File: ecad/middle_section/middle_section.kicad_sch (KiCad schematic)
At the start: 12 parts, among them U1 ADS7830, U2 LM4040DBZ-3

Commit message: [WIP]
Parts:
- removed C1, C3: C_Polarized, Capacitor_SMD:CP_Elec_4x5.7, symbol Device:C_Polarized
- added C1, C3: 2u2, Capacitor_SMD:C_0805_2012Metric, symbol Device:C
- added J1: JST SH, Connector_JST:JST_SH_BM04B-SRSS-TB_1x04-1MP_P1.00mm_Vertical, symbol Connector_Generic:Conn_01x04
- added JP1, JP2: ~, Jumper:SolderJumper-3_P1.3mm_Open_RoundedPad1.0x1.5mm, symbol Jumper:SolderJumper_3_Bridged123
- C2, C4: value C -> 100n
- R1: value R -> 100
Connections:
- net +3V0: now also C1.1
- net +3V3: now also C3.1, J1.1 (Pin_1), JP1.1 (A), JP2.1 (A)
- net GND: now also C1.2, C3.2, J1.4 (Pin_4), JP1.3 (B), JP2.3 (B)
- net A1: now reaches U1.12 (A0)
- net A1: now also JP2.2 (C)
- net A0: now reaches U1.13 (A1)
- net A0: now also JP1.2 (C)
- net SCK: now reaches U1.14 (SCL)
- net SCK: now also J1.3 (Pin_3)
- net SDA: now reaches U1.15 (SDA)
- net SDA: now also J1.2 (Pin_2)

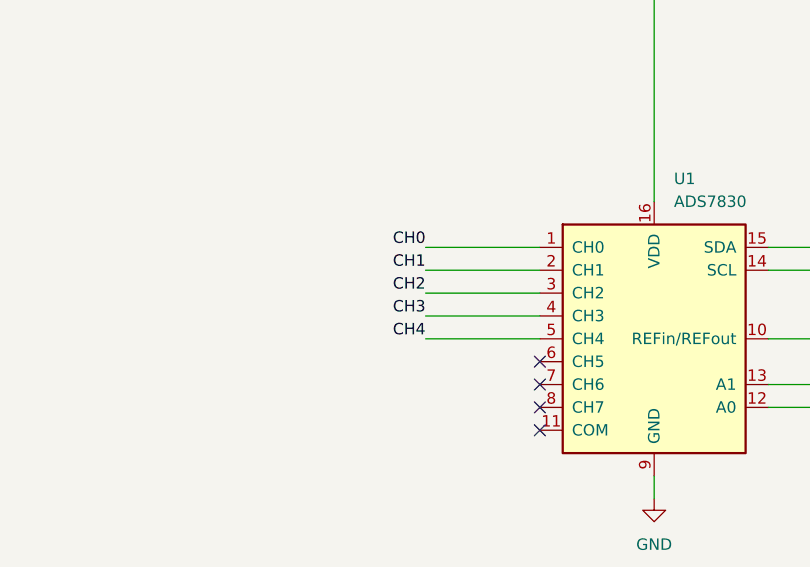
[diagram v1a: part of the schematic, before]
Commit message: Finishes up Middle Section
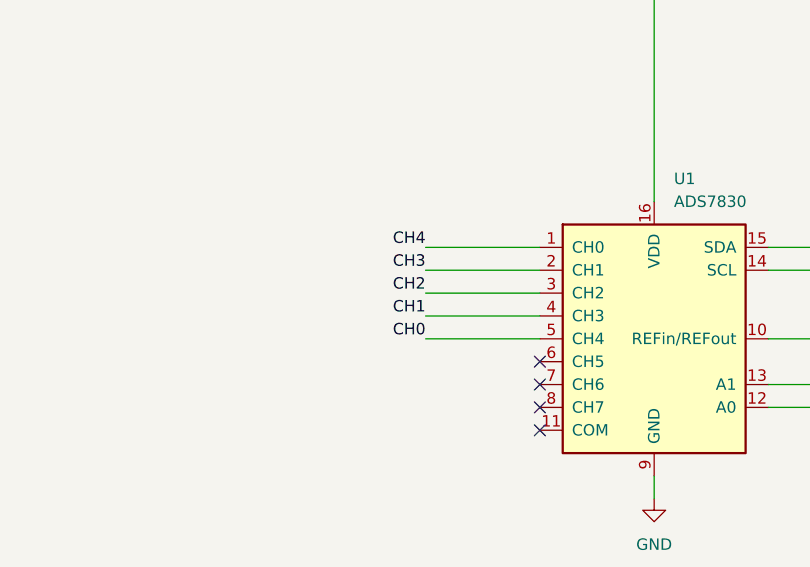
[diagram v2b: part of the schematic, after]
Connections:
- net CH0: now also U1.5 (CH4); no longer U1.1 (CH0)
- net CH1: now also U1.4 (CH3); no longer U1.2 (CH1)
- net CH3: now also U1.2 (CH1); no longer U1.4 (CH3)
- net CH4: now also U1.1 (CH0); no longer U1.5 (CH4)
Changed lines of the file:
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@@
 	)
 	(label "CH3"
-		(at 190.5 58.42 180)
+		(at 190.5 53.34 180)
 		(fields_autoplaced yes)
 		(effects
@@
 	)
 	(label "CH4"
-		(at 190.5 60.96 180)
+		(at 190.5 50.8 180)
 		(fields_autoplaced yes)
 		(effects
@@
 	)
 	(label "CH1"
-		(at 190.5 53.34 180)
+		(at 190.5 58.42 180)
 		(fields_autoplaced yes)
 		(effects
@@
 	)
 	(label "CH0"
-		(at 190.5 50.8 180)
+		(at 190.5 60.96 180)
 		(fields_autoplaced yes)
 		(effects

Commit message: Updates boards
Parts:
- added R2: 100, Resistor_SMD:R_0603_1608Metric, symbol Device:R
- J1: footprint Connector_JST:JST_SH_BM04B-SRSS-TB_1x04-1MP_P1.00mm_Vertical -> woodpecker:JST_SH_BM04B-SRSS-TB_1x04-1MP_P1.00mm_Vertical
- JP1, JP2: footprint Jumper:SolderJumper-3_P1.3mm_Open_RoundedPad1.0x1.5mm -> Jumper:SolderJumper-3_P2.0mm_Open_TrianglePad1.0x1.5mm
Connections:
- net +3V3: now also R2.1; no longer JP1.1 (A), JP2.1 (A)
- new net: JP1.1 (A), JP2.1 (A), R2.2
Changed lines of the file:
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@@
 	)
 	(junction
+		(at 267.97 66.04)
+		(diameter 0)
+		(color 0 0 0 0)
+	)
+	(junction
 		(at 107.95 36.83)
 		(diameter 0)
@@
 	(wire
 		(pts
+			(xy 247.65 66.04) (xy 247.65 76.2)
+		)
+		(stroke
+			(width 0)
+			(type default)
+		)
+	)
+	(wire
+		(pts
 			(xy 151.13 102.87) (xy 154.94 102.87)
 		)
@@
 	(wire
 		(pts
+			(xy 267.97 66.04) (xy 267.97 76.2)
+		)
+		(stroke
+			(width 0)
+			(type default)
+		)
+	)
+	(wire
+		(pts
 			(xy 120.65 110.49) (xy 120.65 106.68)
 		)
@@
 	(wire
 		(pts
-			(xy 228.6 68.58) (xy 234.95 68.58)
+			(xy 247.65 66.04) (xy 267.97 66.04)
 		)
 		(stroke
@@
 	(wire
 		(pts
-			(xy 267.97 72.39) (xy 267.97 76.2)
+			(xy 228.6 68.58) (xy 234.95 68.58)
 		)
 		(stroke
@@
 	(wire
 		(pts
+			(xy 267.97 52.07) (xy 267.97 54.61)
+		)
+		(stroke
+			(width 0)
+			(type default)
+		)
+	)
+	(wire
+		(pts
 			(xy 95.25 95.25) (xy 95.25 99.06)
 		)
@@
 	(wire
 		(pts
-			(xy 247.65 72.39) (xy 247.65 76.2)
-		)
-		(stroke
-			(width 0)
-			(type default)
-		)
-	)
-	(wire
-		(pts
 			(xy 175.26 102.87) (xy 179.07 102.87)
 		)
@@
 	(wire
 		(pts
+			(xy 267.97 66.04) (xy 267.97 62.23)
+		)
+		(stroke
+			(width 0)
+			(type default)
+		)
+	)
+	(wire
+		(pts
 			(xy 215.9 22.86) (xy 242.57 22.86)
 		)
@@
 	(symbol
 		(lib_id "power:+3V3")
-		(at 267.97 72.39 0)
+		(at 267.97 52.07 0)
 		(unit 1)
 		(exclude_from_sim no)
@@
 		(fields_autoplaced yes)
 		(property "Reference" "#PWR022"
-			(at 267.97 76.2 0)
+			(at 267.97 55.88 0)
 			(effects
 				(font
@@
 		)
 		(property "Value" "+3V3"
-			(at 267.97 67.31 0)
+			(at 267.97 46.99 0)
 			(effects
 				(font
@@
 		)
 		(property "Footprint" ""
-			(at 267.97 72.39 0)
+			(at 267.97 52.07 0)
 			(effects
 				(font
@@
 		)
 		(property "Datasheet" ""
-			(at 267.97 72.39 0)
+			(at 267.97 52.07 0)
 			(effects
 				(font
@@
 		)
 		(property "Description" "Power symbol creates a global label with name \"+3V3\""
-			(at 267.97 72.39 0)
+			(at 267.97 52.07 0)
 			(effects
 				(font
@@
 	)
 	(symbol
-		(lib_id "power:+3V3")
-		(at 247.65 72.39 0)
+		(lib_id "Jumper:SolderJumper_3_Bridged123")
+		(at 267.97 81.28 270)
 		(unit 1)
 		(exclude_from_sim no)
@@
 		(dnp no)
 		(fields_autoplaced yes)
-		(property "Reference" "#PWR021"
-			(at 247.65 76.2 0)
+		(property "Reference" "JP2"
+			(at 270.51 80.0099 90)
 			(effects
 				(font
 					(size 1.27 1.27)
 				)
-				(hide yes)
+				(justify left)
 			)
 		)
-		(property "Value" "+3V3"
-			(at 247.65 67.31 0)
+		(property "Value" "~"
+			(at 270.51 82.5499 90)
 			(effects
 				(font
 					(size 1.27 1.27)
 				)
+				(justify left)
+				(hide yes)
 			)
 		)
-		(property "Footprint" ""
-			(at 247.65 72.39 0)
+		(property "Footprint" "Jumper:SolderJumper-3_P2.0mm_Open_TrianglePad1.0x1.5mm"
+			(at 267.97 81.28 0)
 			(effects
 				(font
@@
 			)
 		)
-		(property "Datasheet" ""
-			(at 247.65 72.39 0)
+		(property "Datasheet" "~"
+			(at 267.97 81.28 0)
 			(effects
 				(font
@@
 			)
 		)
-		(property "Description" "Power symbol creates a global label with name \"+3V3\""
-			(at 247.65 72.39 0)
+		(property "Description" "Solder Jumper, 3-pole, pins 1+2+3 closed/bridged"
+			(at 267.97 81.28 0)
 			(effects
 				(font
@@
 			)
 		)
+		(pin "3"
+		)
 		(pin "1"
 		)
+		(pin "2"
+		)
 		(instances
 			(project "middle_section"
 				(path "/15a112d2-e643-4be2-b8ef-4d676777cd27"
-					(reference "#PWR021")
+					(reference "JP2")
 					(unit 1)
 				)
@@
 	)
 	(symbol
-		(lib_id "Jumper:SolderJumper_3_Bridged123")
-		(at 267.97 81.28 270)
+		(lib_id "power:+3V0")
+		(at 147.32 95.25 0)
 		(unit 1)
 		(exclude_from_sim no)
@@
 		(dnp no)
 		(fields_autoplaced yes)
-		(property "Reference" "JP2"
-			(at 270.51 80.0099 90)
+		(property "Reference" "#PWR017"
+			(at 147.32 99.06 0)
 			(effects
 				(font
 					(size 1.27 1.27)
 				)
-				(justify left)
+				(hide yes)
 			)
 		)
-		(property "Value" "~"
-			(at 270.51 82.5499 90)
+		(property "Value" "+3V0"
+			(at 147.32 90.17 0)
 			(effects
 				(font
 					(size 1.27 1.27)
 				)
-				(justify left)
-				(hide yes)
 			)
 		)
-		(property "Footprint" "Jumper:SolderJumper-3_P1.3mm_Open_RoundedPad1.0x1.5mm"
-			(at 267.97 81.28 0)
+		(property "Footprint" ""
+			(at 147.32 95.25 0)
 			(effects
 				(font
@@
 			)
 		)
-		(property "Datasheet" "~"
-			(at 267.97 81.28 0)
+		(property "Datasheet" ""
+			(at 147.32 95.25 0)
 			(effects
 				(font
@@
 			)
 		)
-		(property "Description" "Solder Jumper, 3-pole, pins 1+2+3 closed/bridged"
-			(at 267.97 81.28 0)
+		(property "Description" "Power symbol creates a global label with name \"+3V0\""
+			(at 147.32 95.25 0)
 			(effects
 				(font
@@
 			)
 		)
-		(pin "3"
-		)
 		(pin "1"
 		)
-		(pin "2"
-		)
 		(instances
 			(project "middle_section"
 				(path "/15a112d2-e643-4be2-b8ef-4d676777cd27"
-					(reference "JP2")
+					(reference "#PWR017")
 					(unit 1)
 				)
@@
 	(symbol
 		(lib_id "power:+3V0")
-		(at 147.32 95.25 0)
+		(at 137.16 22.86 0)
 		(unit 1)
 		(exclude_from_sim no)
@@
 		(dnp no)
 		(fields_autoplaced yes)
-		(property "Reference" "#PWR017"
-			(at 147.32 99.06 0)
+		(property "Reference" "#PWR09"
+			(at 137.16 26.67 0)
 			(effects
 				(font
@@
 		)
 		(property "Value" "+3V0"
-			(at 147.32 90.17 0)
+			(at 137.16 17.78 0)
 			(effects
 				(font
@@
 		)
 		(property "Footprint" ""
-			(at 147.32 95.25 0)
+			(at 137.16 22.86 0)
 			(effects
 				(font
@@
 		)
 		(property "Datasheet" ""
-			(at 147.32 95.25 0)
+			(at 137.16 22.86 0)
 			(effects
 				(font
@@
 		)
 		(property "Description" "Power symbol creates a global label with name \"+3V0\""
-			(at 147.32 95.25 0)
+			(at 137.16 22.86 0)
 			(effects
 				(font
@@
 			(project "middle_section"
 				(path "/15a112d2-e643-4be2-b8ef-4d676777cd27"
-					(reference "#PWR017")
+					(reference "#PWR09")
 					(unit 1)
 				)
@@
 	(symbol
 		(lib_id "power:+3V0")
-		(at 137.16 22.86 0)
+		(at 120.65 95.25 0)
 		(unit 1)
 		(exclude_from_sim no)
@@
 		(dnp no)
 		(fields_autoplaced yes)
-		(property "Reference" "#PWR09"
-			(at 137.16 26.67 0)
+		(property "Reference" "#PWR015"
+			(at 120.65 99.06 0)
 			(effects
 				(font
@@
 		)
 		(property "Value" "+3V0"
-			(at 137.16 17.78 0)
+			(at 120.65 90.17 0)
 			(effects
 				(font
@@
 		)
 		(property "Footprint" ""
-			(at 137.16 22.86 0)
+			(at 120.65 95.25 0)
 			(effects
 				(font
@@
 		)
 		(property "Datasheet" ""
-			(at 137.16 22.86 0)
+			(at 120.65 95.25 0)
 			(effects
 				(font
@@
 		)
 		(property "Description" "Power symbol creates a global label with name \"+3V0\""
-			(at 137.16 22.86 0)
+			(at 120.65 95.25 0)
 			(effects
 				(font
@@
 			(project "middle_section"
 				(path "/15a112d2-e643-4be2-b8ef-4d676777cd27"
-					(reference "#PWR09")
+					(reference "#PWR015")
 					(unit 1)
 				)
@@
 	)
 	(symbol
-		(lib_id "power:+3V0")
-		(at 120.65 95.25 0)
+		(lib_id "Device:R")
+		(at 267.97 58.42 0)
 		(unit 1)
 		(exclude_from_sim no)
@@
 		(dnp no)
 		(fields_autoplaced yes)
-		(property "Reference" "#PWR015"
-			(at 120.65 99.06 0)
+		(property "Reference" "R2"
+			(at 270.51 57.1499 0)
 			(effects
 				(font
 					(size 1.27 1.27)
 				)
-				(hide yes)
+				(justify left)
 			)
 		)
-		(property "Value" "+3V0"
-			(at 120.65 90.17 0)
+		(property "Value" "100"
+			(at 270.51 59.6899 0)
 			(effects
 				(font
 					(size 1.27 1.27)
 				)
+				(justify left)
 			)
 		)
-		(property "Footprint" ""
-			(at 120.65 95.25 0)
+		(property "Footprint" "Resistor_SMD:R_0603_1608Metric"
+			(at 266.192 58.42 90)
 			(effects
 				(font
@@
 			)
 		)
-		(property "Datasheet" ""
-			(at 120.65 95.25 0)
+		(property "Datasheet" "~"
+			(at 267.97 58.42 0)
 			(effects
 				(font
@@
 			)
 		)
-		(property "Description" "Power symbol creates a global label with name \"+3V0\""
-			(at 120.65 95.25 0)
+		(property "Description" "Resistor"
+			(at 267.97 58.42 0)
 			(effects
 				(font
@@
 		(pin "1"
 		)
+		(pin "2"
+		)
 		(instances
 			(project "middle_section"
 				(path "/15a112d2-e643-4be2-b8ef-4d676777cd27"
-					(reference "#PWR015")
+					(reference "R2")
 					(unit 1)
 				)
@@
 			)
 		)
-		(property "Footprint" "Connector_JST:JST_SH_BM04B-SRSS-TB_1x04-1MP_P1.00mm_Vertical"
+		(property "Footprint" "woodpecker:JST_SH_BM04B-SRSS-TB_1x04-1MP_P1.00mm_Vertical"
 			(at 210.82 111.76 0)
 			(effects
@@
 			)
 		)
-		(property "Footprint" "Jumper:SolderJumper-3_P1.3mm_Open_RoundedPad1.0x1.5mm"
+		(property "Footprint" "Jumper:SolderJumper-3_P2.0mm_Open_TrianglePad1.0x1.5mm"
 			(at 247.65 81.28 0)
 			(effects

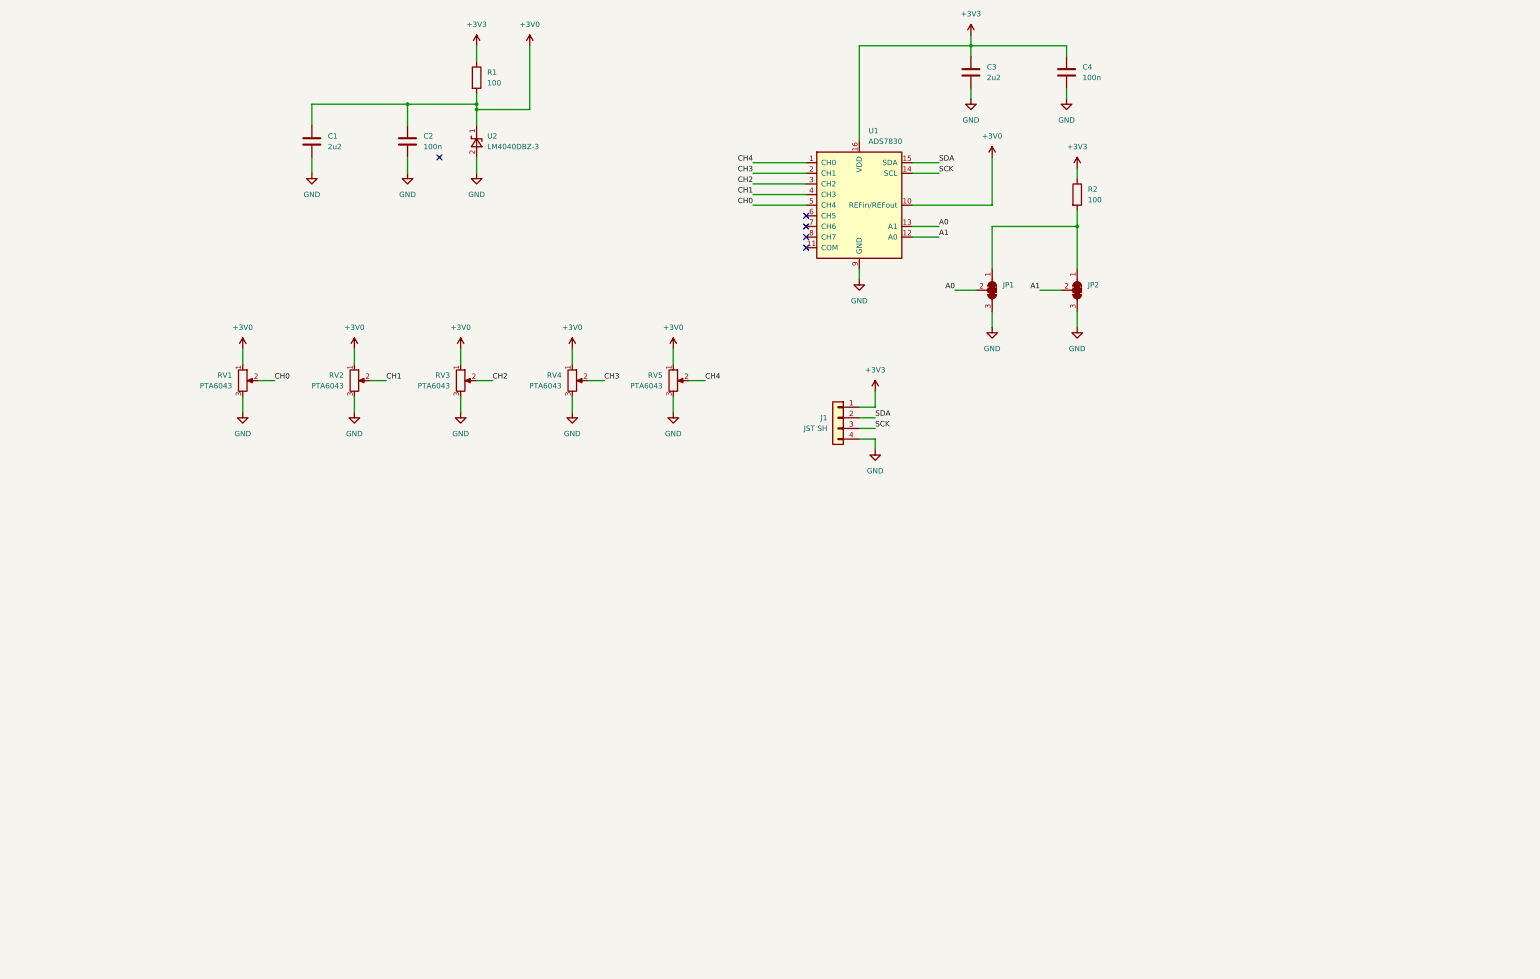
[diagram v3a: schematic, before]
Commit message: Uses Attiny1617 MCU for ADC & Matrix RO
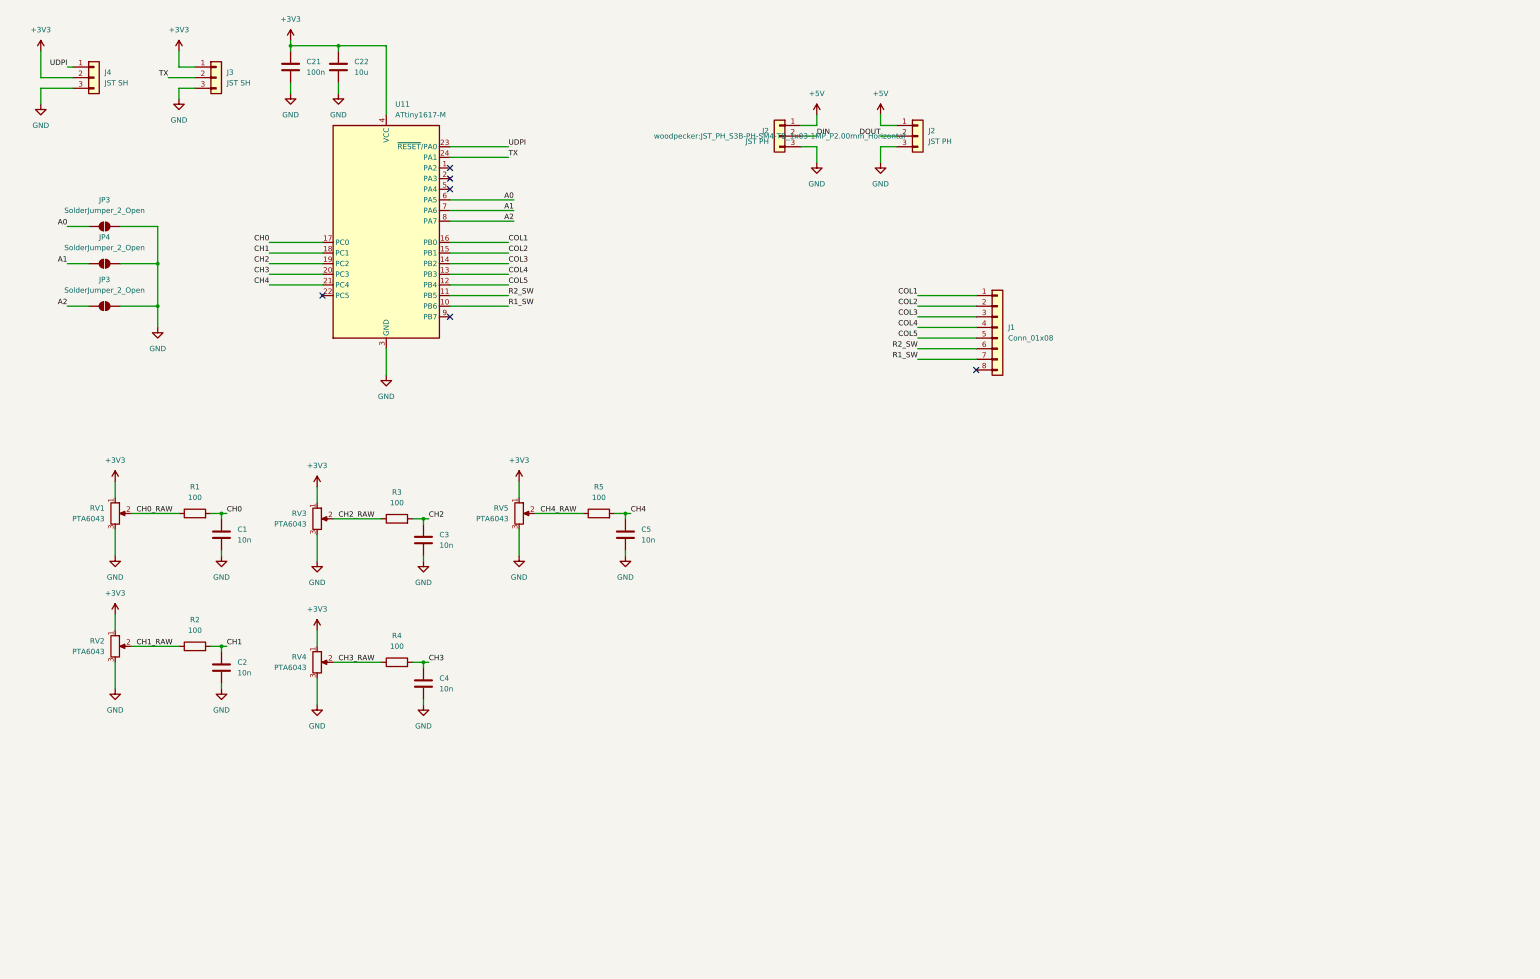
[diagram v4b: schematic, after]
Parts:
- removed J1: JST SH, woodpecker:JST_SH_BM04B-SRSS-TB_1x04-1MP_P1.00mm_Vertical, symbol Connector_Generic:Conn_01x04
- removed JP1, JP2: ~, Jumper:SolderJumper-3_P2.0mm_Open_TrianglePad1.0x1.5mm, symbol Jumper:SolderJumper_3_Bridged123
- removed U1: ADS7830, Package_SO:TSSOP-16_4.4x5mm_P0.65mm, symbol Analog_DAC:ADS7830
- removed U2: LM4040DBZ-3, Package_TO_SOT_SMD:SOT-23, symbol Reference_Voltage:LM4040DBZ-3
- added C21: 100n, Capacitor_SMD:C_0603_1608Metric, symbol Device:C
- added C22: 10u, Capacitor_SMD:C_0603_1608Metric, symbol Device:C
- added C5: 10n, Capacitor_SMD:C_0603_1608Metric, symbol Device:C
- added J1: Conn_01x08, symbol Connector_Generic:Conn_01x08
- added J2 (x2): JST PH, woodpecker:JST_PH_S3B-PH-SM4-TB_1x03-1MP_P2.00mm_Horizontal, symbol Connector_Generic:Conn_01x03
- added J3, J4: JST SH, woodpecker:JST_SH_BM03B-SRSS-TB_1x03-1MP_P1.00mm_Vertical, symbol Connector_Generic:Conn_01x03
- added JP3 (x2), JP4: SolderJumper_2_Open, Jumper:SolderJumper-2_P1.3mm_Open_TrianglePad1.0x1.5mm, symbol Jumper:SolderJumper_2_Open
- added R3, R4, R5: 100, Resistor_SMD:R_0603_1608Metric, symbol Device:R
- added U11: ATtiny1617-M, Package_DFN_QFN:QFN-24-1EP_4x4mm_P0.5mm_EP2.6x2.6mm, symbol MCU_Microchip_ATtiny:ATtiny1617-M
- C1, C3: value 2u2 -> 10n; footprint Capacitor_SMD:C_0805_2012Metric -> Capacitor_SMD:C_0603_1608Metric
- C2, C4: value 100n -> 10n
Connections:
- net +3V3: now also RV1.1, RV2.1, RV3.1, RV4.1, RV5.1, C21.1, C22.1, J3.1 (Pin_1), J4.2 (Pin_2), U11.4 (VCC); no longer C3.1, C4.1, R1.1, R2.1
- net A0: now also JP3.1 (A), U11.6 (PA5)
- net A1: now also JP4.1 (A), U11.7 (PA6)
- net CH0: now also C1.1, R1.2, U11.17 (PC0); no longer RV1.2
- net CH1: now also C2.1, R2.2, U11.18 (PC1); no longer RV2.2
- net CH2: now also C3.1, R3.2, U11.19 (PC2); no longer RV3.2
- net CH3: now also C4.1, R4.2, U11.20 (PC3); no longer RV4.2
- net CH4: now also C5.1, R5.2, U11.21 (PC4); no longer RV5.2
- net GND: now also C21.2, C22.2, C5.2, J2.3 (Pin_3), J2.3 (Pin_3), J3.3 (Pin_3), J4.3 (Pin_3), JP3.2 (B), JP3.2 (B), JP4.2 (B), U11.25 (GND), U11.3 (GND)
- removed net +3V0: C1.1, C2.1, R1.2, RV1.1, RV2.1, RV3.1, RV4.1, RV5.1
- new net +5V: J2.1 (Pin_1), J2.1 (Pin_1)
- new net A2: JP3.1 (A), U11.8 (PA7)
- new net CH0_RAW: R1.1, RV1.2
- new net CH1_RAW: R2.1, RV2.2
- new net CH2_RAW: R3.1, RV3.2
- new net CH3_RAW: R4.1, RV4.2
- new net CH4_RAW: R5.1, RV5.2
- new net COL1: J1.1 (Pin_1), U11.16 (PB0)
- new net COL2: J1.2 (Pin_2), U11.15 (PB1)
- new net COL3: J1.3 (Pin_3), U11.14 (PB2)
- new net COL4: J1.4 (Pin_4), U11.13 (PB3)
- new net COL5: J1.5 (Pin_5), U11.12 (PB4)
- new net DIN: J2.2 (Pin_2)
- new net DOUT: J2.2 (Pin_2)
- new net R1_SW: J1.7 (Pin_7), U11.10 (PB6)
- new net R2_SW: J1.6 (Pin_6), U11.11 (PB5)
- new net TX: J3.2 (Pin_2), U11.24 (PA1)
- new net UDPI: J4.1 (Pin_1), U11.23 (~{RESET}/PA0)
- no-connect marks 5 -> 6
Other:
- moved on the sheet: RV1
